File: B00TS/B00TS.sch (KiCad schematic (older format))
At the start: 10 parts

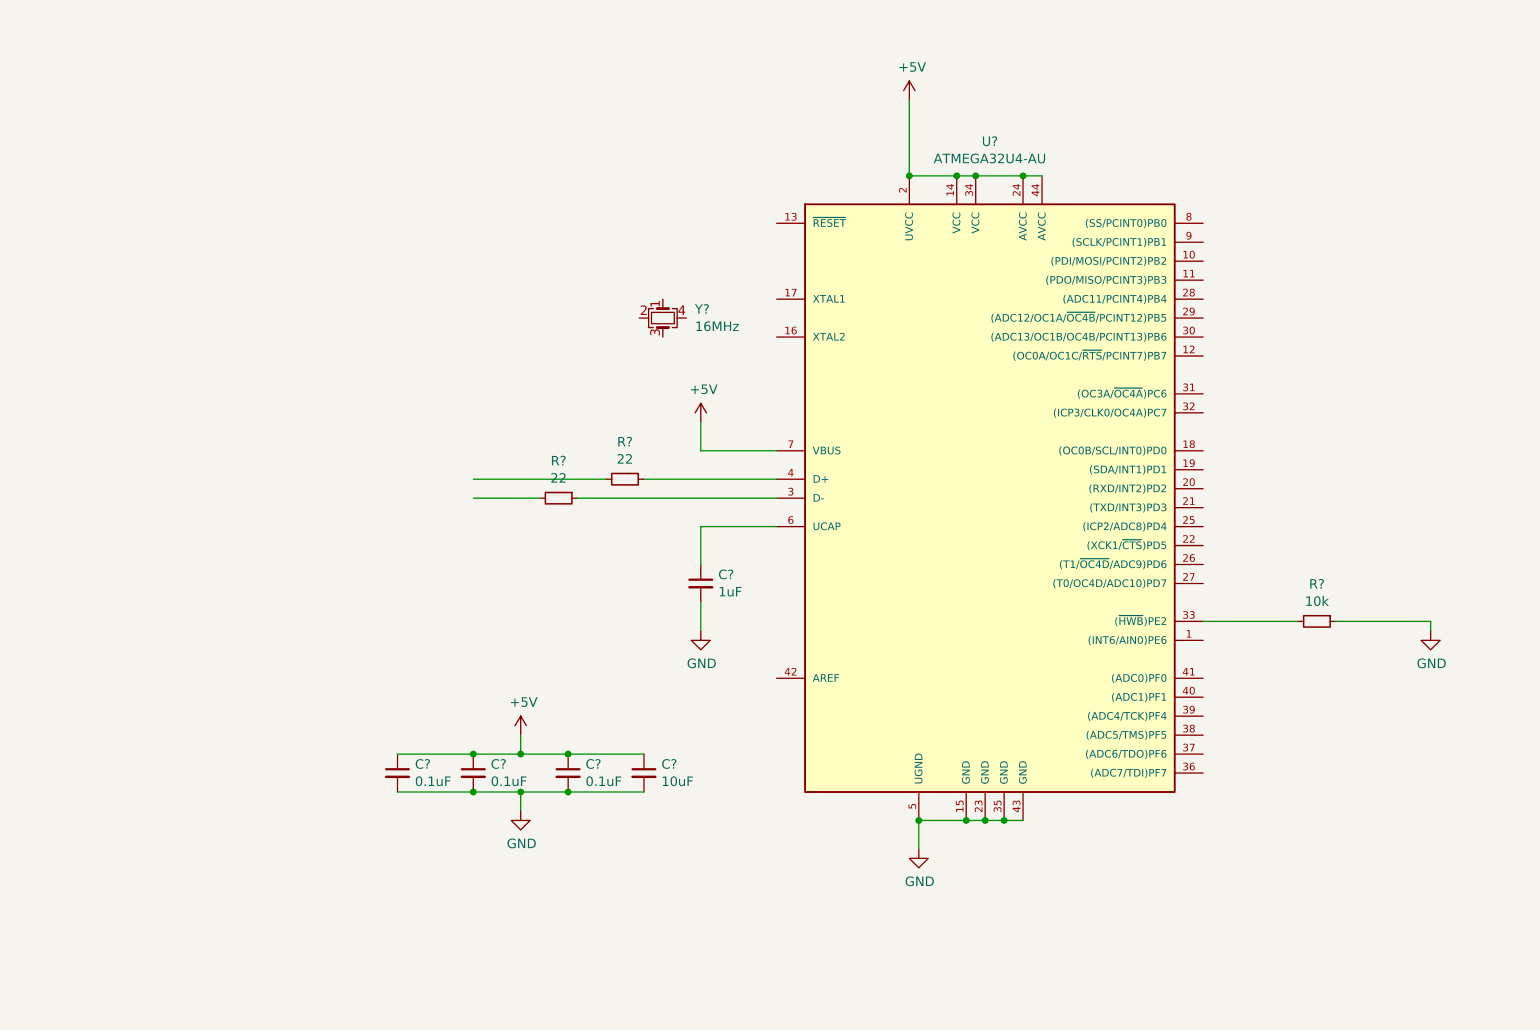
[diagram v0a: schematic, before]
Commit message: Assigned schematics to footprints
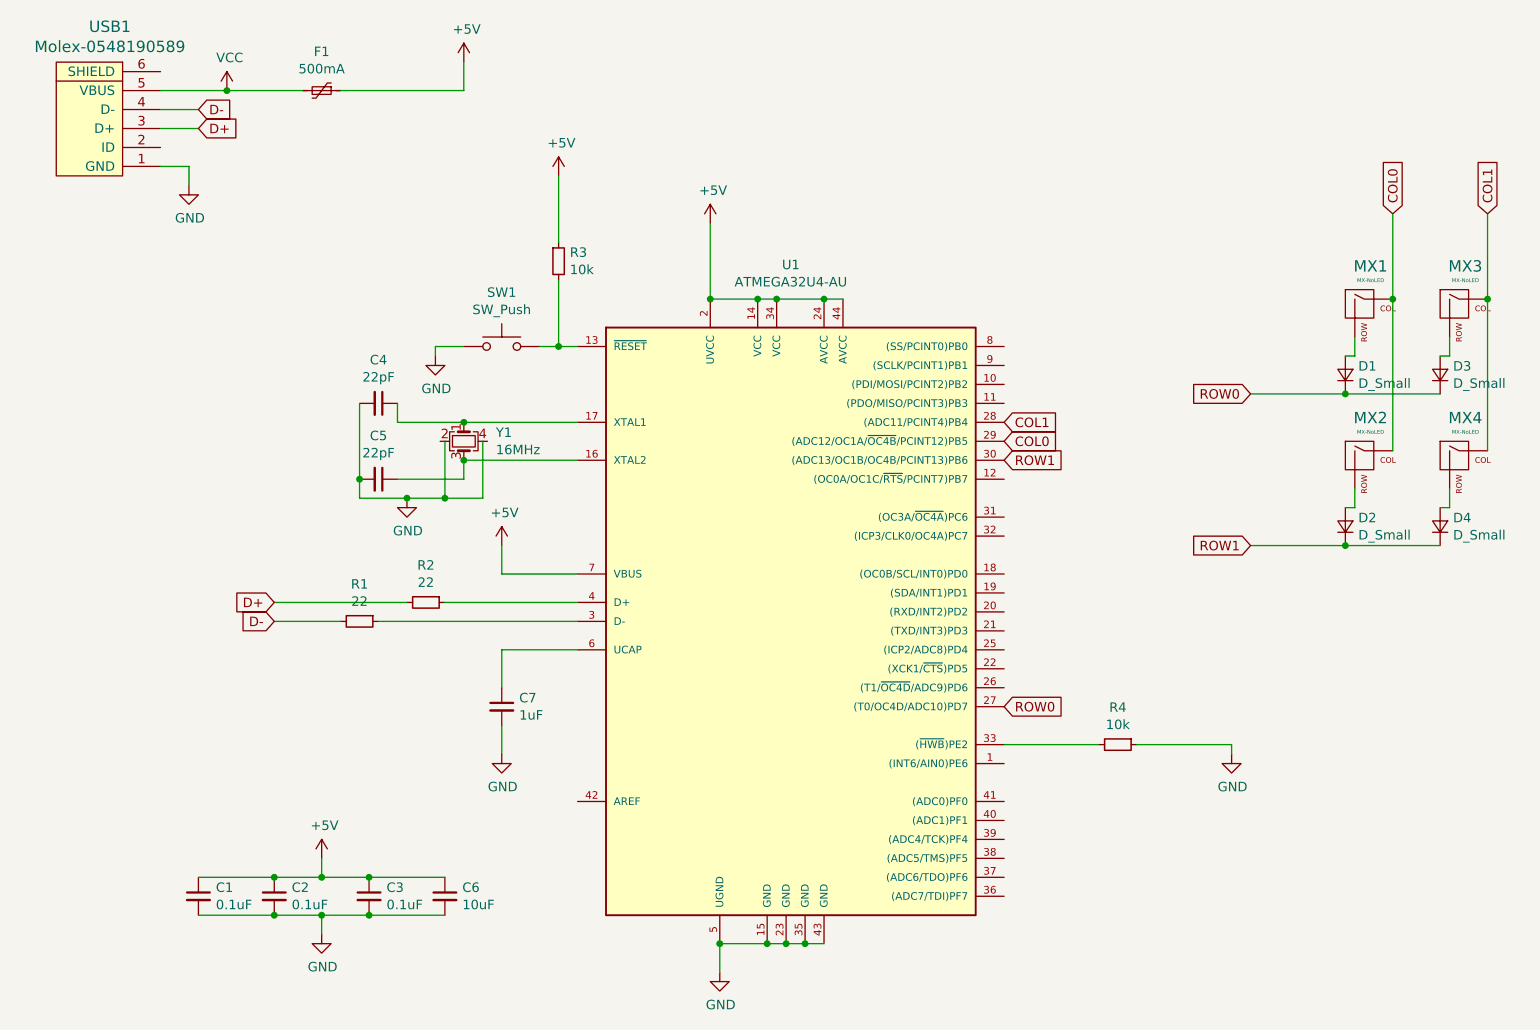
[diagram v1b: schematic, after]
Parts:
- added C4, C5: 22pF, Capacitor_SMD:C_0805_2012Metric_Pad1.15x1.40mm_HandSolder, symbol device:C_Small
- added D1, D2, D3, D4: D_Small, Diode_SMD:D_SOD-123, symbol device:D_Small
- added F1: 500mA, Fuse:Fuse_1206_3216Metric, symbol device:Polyfuse_Small
- added MX1, MX2, MX3, MX4: MX-NoLED, MX_Alps_Hybrid:MX-1U-NoLED, symbol MX_Alps_Hybrid:MX-NoLED
- added R3: 10k, Resistor_SMD:R_0805_2012Metric_Pad1.15x1.40mm_HandSolder, symbol device:R_Small
- added SW1: SW_Push, random-keyboard-parts:SKQG-1155865, symbol Switch:SW_Push
- added USB1: Molex-0548190589, random-keyboard-parts:Molex-0548190589, symbol random-keyboard-parts:Molex-0548190589
- C1, C2, C3, C6, C7: renamed from C?; footprint (none) -> Capacitor_SMD:C_0805_2012Metric_Pad1.15x1.40mm_HandSolder
- R1, R2, R4: renamed from R?; footprint (none) -> Resistor_SMD:R_0805_2012Metric_Pad1.15x1.40mm_HandSolder
- U1: renamed from U?; footprint TQFP44 -> Package_QFP:TQFP-44_10x10mm_P0.8mm
- Y1: renamed from Y?; footprint (none) -> Crystal:Crystal_SMD_3225-4Pin_3.2x2.5mm_HandSoldering
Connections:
- net labels added: COL0, COL1, D+, D-, ROW0, ROW1, VCC
- wire segments 32 -> 75
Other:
- moved on the sheet: C1, C2, C3, C6, C7, R1, R2, R4, U1, Y1
